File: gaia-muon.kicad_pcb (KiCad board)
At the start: 8 copper layers, 50 x 50 mm, 89 parts, among them J1 Conn_02x10_Odd_Even, J2 Conn_02x10_Odd_Even, J3 Debug_Conn, J4 Conn_01x04_Pin, Q1 2N7002, SW1 SW_Push, U1 MAX5026, U2 TPH2502, U3 TPH2502, U4 LM4040DBZ-2.5, U5 W25Q128JVS, U7 MICROFC-60035-SIPM, U8 RP2040, U9 AP2112K-3.3, Y1 AMB8-272-T3

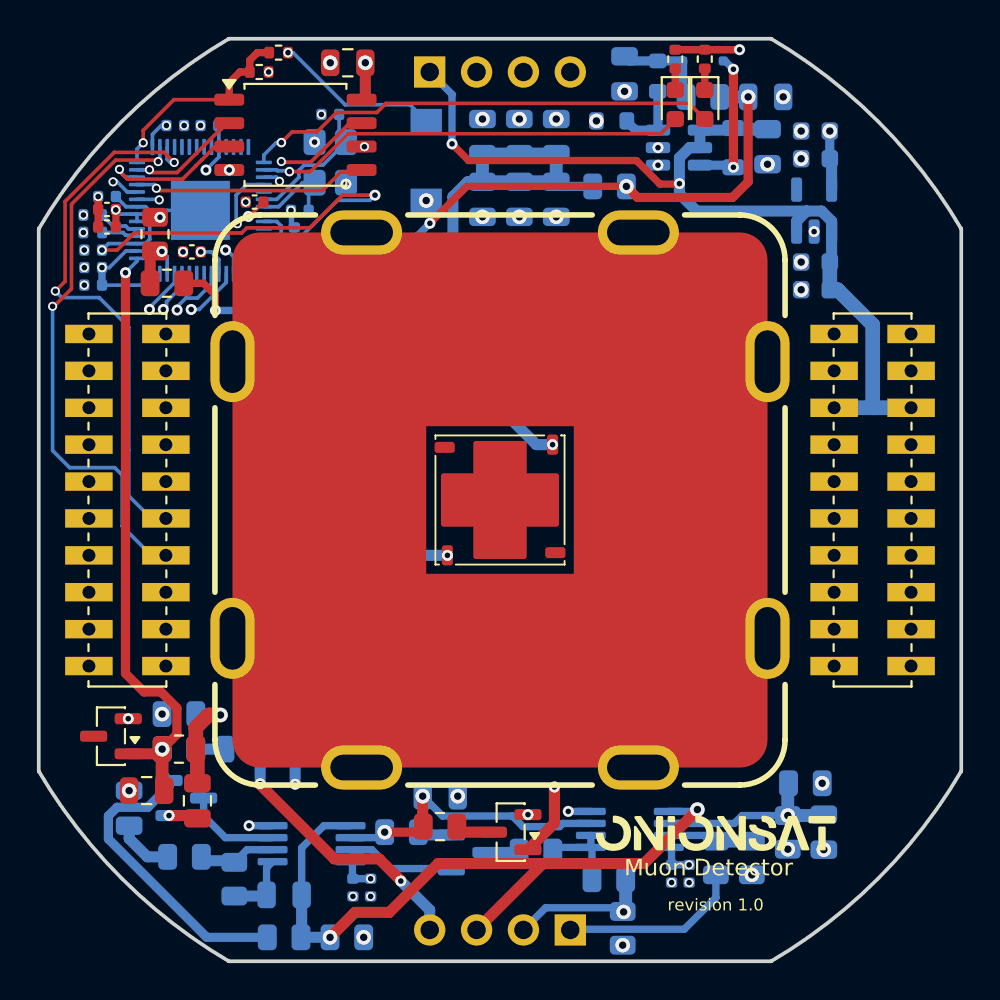
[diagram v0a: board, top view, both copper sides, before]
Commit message: removing 2 layers (8->6 layers)
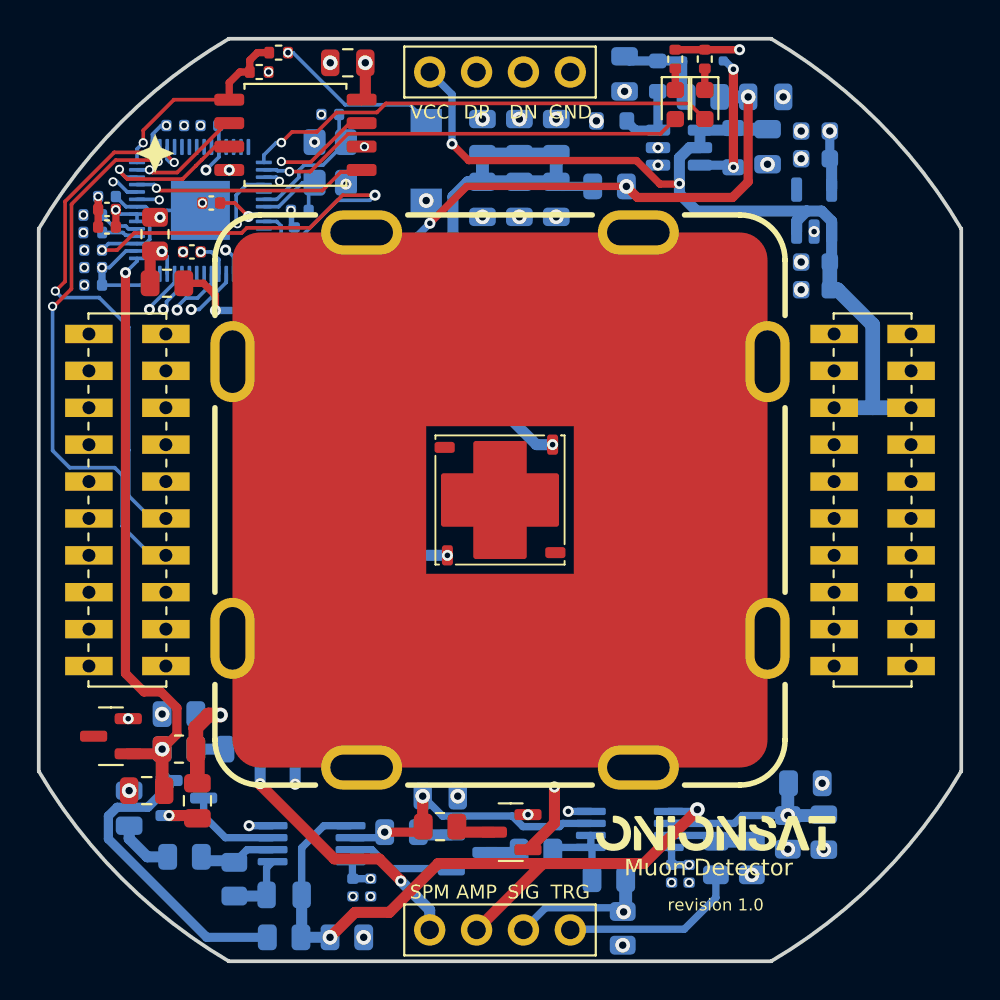
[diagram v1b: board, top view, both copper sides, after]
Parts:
- D2, D3, Q1, U4: footprint Package_TO_SOT_SMD:SOT-23 -> gaia-muon-footprints:SOT-23
- J3, J4: footprint Connector_PinHeader_2.54mm:PinHeader_1x04_P2.54mm_Vertical -> gaia-muon-footprints:PinHeader_1x04_P2.54mm_Vertical
- U1: footprint Package_TO_SOT_SMD:SOT-23-6 -> gaia-muon-footprints:SOT-23-6
- U2, U3: footprint Package_SO:MSOP-8_3x3mm_P0.65mm -> gaia-muon-footprints:MSOP-8_3x3mm_P0.65mm
- U5: footprint Package_SO:SOIC-8_5.3x5.3mm_P1.27mm -> gaia-muon-footprints:SOIC-8_5.3x5.3mm_P1.27mm
- U8: footprint Package_DFN_QFN:QFN-56-1EP_7x7mm_P0.4mm_EP3.2x3.2mm -> gaia-muon-footprints:QFN-56-1EP_7x7mm_P0.4mm_EP3.2x3.2mm
- U9: footprint Package_TO_SOT_SMD:SOT-23-5 -> gaia-muon-footprints:SOT-23-5
- Y1: footprint Crystal:Crystal_SMD_3225-4Pin_3.2x2.5mm -> gaia-muon-footprints:Crystal_SMD_3225-4Pin_3.2x2.5mm
- moved C35 2.35 mm to (149.3, 84.6)
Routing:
- net +3.3V: track 30.8 -> 31.5 mm
- removed copper zone on In6.Cu, net GND
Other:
- copper layers 8 -> 6
- board text added: "AMP"
- board text added: "DN"
- board text added: "DP"
- board text added: "GND"
- board text added: "SIG"
- board text added: "SPM"
- board text added: "TRG"
- board text added: "VCC"

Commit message: Production start
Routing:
- net VRef: track 51.3 -> 45.2 mm, vias 2 -> 3

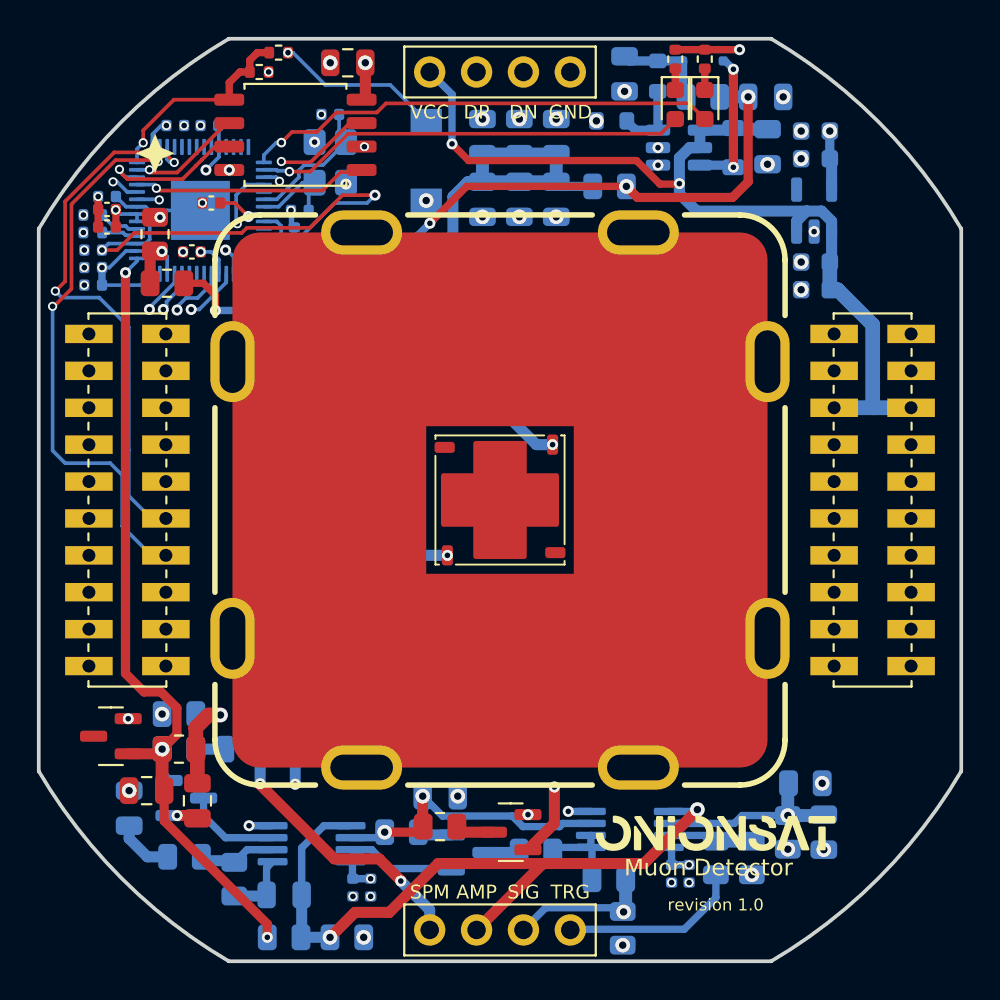
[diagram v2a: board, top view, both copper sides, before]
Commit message: adding stitching vias
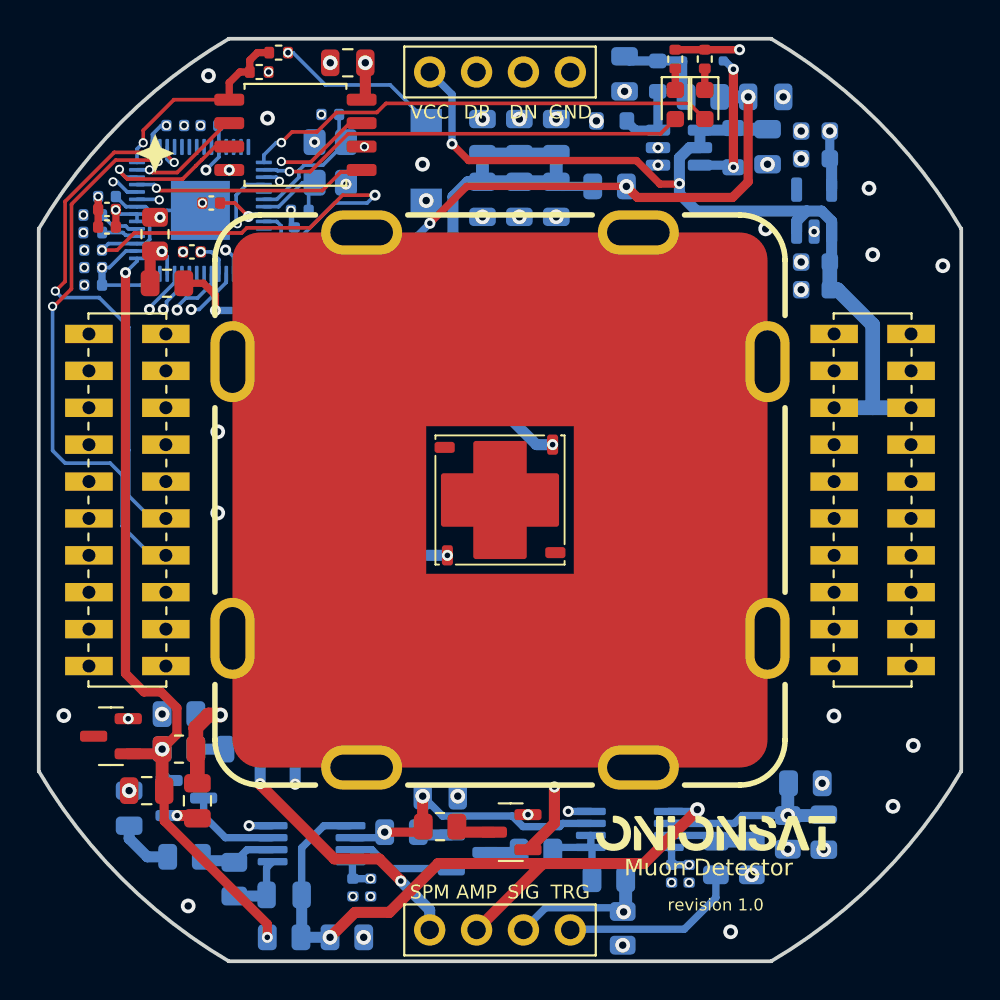
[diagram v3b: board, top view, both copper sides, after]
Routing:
- net GND: vias 52 -> 67
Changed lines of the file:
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@@
+	)
+	(via
+		(at 149.7 101.4)
+		(size 0.8)
+		(drill 0.4)
+		(layers "F.Cu" "B.Cu")
+		(free yes)
+		(net 1)
 	)
 	(via
@@
 	)
 	(via
+		(at 177.5 124.1)
+		(size 0.8)
+		(drill 0.4)
+		(layers "F.Cu" "B.Cu")
+		(free yes)
+		(net 1)
+	)
+	(via
 		(at 148.87 84.6)
 		(size 0.5)
@@
 	)
 	(via
+		(at 187.4 114)
+		(size 0.8)
+		(drill 0.4)
+		(layers "F.Cu" "B.Cu")
+		(free yes)
+		(net 1)
+	)
+	(via
 		(at 157.9875 122.1825)
 		(size 0.5)
@@
 	)
 	(via
+		(at 160.8 82.5)
+		(size 0.8)
+		(drill 0.4)
+		(layers "F.Cu" "B.Cu")
+		(free yes)
+		(net 1)
+	)
+	(via
 		(at 153.67 85)
 		(size 0.5)
@@
 	)
 	(via
+		(at 179.4 86)
+		(size 0.8)
+		(drill 0.4)
+		(layers "F.Cu" "B.Cu")
+		(free yes)
+		(net 1)
+	)
+	(via
 		(at 146.571475 85.371475)
 		(size 0.6)
@@
 	)
 	(via
+		(at 152.4 80)
+		(size 0.8)
+		(drill 0.4)
+		(layers "F.Cu" "B.Cu")
+		(free yes)
+		(net 1)
+	)
+	(via
 		(at 142.47 87.15)
 		(size 0.5)
@@
 	)
 	(via
+		(at 185 83.8)
+		(size 0.8)
+		(drill 0.4)
+		(layers "F.Cu" "B.Cu")
+		(free yes)
+		(net 1)
+	)
+	(via
 		(at 168.7 117.575)
 		(size 0.6)
@@
 	)
 	(via
+		(at 149.2 77.7)
+		(size 0.8)
+		(drill 0.4)
+		(layers "F.Cu" "B.Cu")
+		(free yes)
+		(net 1)
+	)
+	(via
+		(at 141.35687 112.381779)
+		(size 0.8)
+		(drill 0.4)
+		(layers "F.Cu" "B.Cu")
+		(free yes)
+		(net 1)
+	)
+	(via
 		(at 153.9 116.1)
 		(size 0.6)
@@
 	)
 	(via
+		(at 149.7 97)
+		(size 0.8)
+		(drill 0.4)
+		(layers "F.Cu" "B.Cu")
+		(free yes)
+		(net 1)
+	)
+	(via
 		(at 155.32 79.8)
 		(size 0.5)
@@
 	)
 	(via
+		(at 189 88)
+		(size 0.8)
+		(drill 0.4)
+		(layers "F.Cu" "B.Cu")
+		(free yes)
+		(net 1)
+	)
+	(via
+		(at 148.1 122.7)
+		(size 0.8)
+		(drill 0.4)
+		(layers "F.Cu" "B.Cu")
+		(free yes)
+		(net 1)
+	)
+	(via
 		(at 179.5 82.5)
 		(size 0.8)
@@
 		(drill 0.3)
 		(layers "F.Cu" "B.Cu")
+		(net 1)
+	)
+	(via
+		(at 186.3 117.3)
+		(size 0.8)
+		(drill 0.4)
+		(layers "F.Cu" "B.Cu")
+		(free yes)
 		(net 1)
 	)
@@
 	)
 	(via
+		(at 183.1 112.4)
+		(size 0.8)
+		(drill 0.4)
+		(layers "F.Cu" "B.Cu")
+		(free yes)
+		(net 1)
+	)
+	(via
 		(at 144.9 116.45)
 		(size 0.8)
@@
 		(net 1)
 	)
+	(via
+		(at 185.2 87.4)
+		(size 0.8)
+		(drill 0.4)
+		(layers "F.Cu" "B.Cu")
+		(free yes)
+		(net 1)
+	)
